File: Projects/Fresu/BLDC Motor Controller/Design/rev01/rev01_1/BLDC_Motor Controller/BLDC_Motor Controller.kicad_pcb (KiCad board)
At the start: 4 copper layers, 100 x 75 mm, 178 parts, among them CN1 XT60PW-M, J1 Conn_01x08, J2 Conn_01x06, J3 Conn_01x03, J4 7461084, J5 7461084, J6 7461084, J7 Conn_01x06, J8 XH-2PWBPZ, J9 TYPE-C-31-M-12, Q1 HSBA15810C, Q2 HSBA15810C, Q3 HSBA15810C, Q4 HSBA15810C, Q5 HSBA15810C, Q6 HSBA15810C, SW1 PTS526SK15SMTR2LFS, U1 STM32F405RGTx, U2 DRV8302_DCA_56, U3 S4B-XH-SM4-TB-(LF)(SN), U4 SN65HVD230, U5 AMS1117-3.3, U6 PUSB3AB6Z, Y1 8MHz

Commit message: Update 22
Continued DRC
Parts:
- C56: moved to B.Cu
- moved C56 0.78 mm to (238.6, 119.6)
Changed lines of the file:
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@@
     (pad "2" thru_hole circle locked (at 5.643701 0.113589 180) (size 2.2 2.2) (drill 1.2) (layers "*.Cu" "*.Mask")
       (net 2 "GND") (pinfunction "2") (pintype "passive"))
-    (model "C:/Users/Will/Downloads/Libraries (1)/Libraries/3D Models/CAP_LAT_SIDE.step"
+    (model "C:/Users/Will/Downloads/Libraries (1)/Libraries/3D Models/CAP_LAT_SIDE.step" hide
       (offset (xyz 1.9 -5.1 9.5))
       (scale (xyz 2.5 2.5 2.5))
@@
       (net 62 "H3_LOW") (pinfunction "2") (pintype "passive"))
   )
-  (footprint "DF_ESC_Footprint_Library:CAP-TH_BD18.0-P7.50-D1.2-SIDE" (layer "F.Cu")
-    (at 237.871 120.015 180)
-    (descr "CAP-TH_BD18.0-P7.50-D1.2-FD footprint")
-    (tags "CAP-TH_BD18.0-P7.50-D1.2-FD footprint")
-    (property "Capacitance" "820uF")
-    (property "LCSC" "C443097")
-    (property "Sheetfile" "INPUT PROTECTION.kicad_sch")
-    (property "Sheetname" "INPUT PROTECTION")
-    (property "ki_keywords" "C443097")
-    (attr through_hole)
-    (fp_text reference "C56" (at 2 -8.5) (layer "F.SilkS")
-        (effects (font (size 1 1) (thickness 0.15)))
-    )
-    (fp_text value "LKMI2501K821MF" (at 0 2.863602) (layer "F.Fab")
-        (effects (font (size 1 1) (thickness 0.15)))
-    )
-    (fp_text user "REF**" (at 0 4.863602) (layer "F.Fab")
-        (effects (font (size 1 1) (thickness 0.15)))
-    )
-    (fp_line (start -7.6 36) (end -7.6 4.5)
-      (stroke (width 0.12) (type solid)) (layer "F.SilkS"))
-    (fp_line (start -1.9 -2.536398) (end -1.9 -4.263602)
-      (stroke (width 0.254) (type solid)) (layer "F.SilkS"))
-    (fp_line (start -1.010998 -3.3746) (end -2.687402 -3.3746)
-      (stroke (width 0.254) (type solid)) (layer "F.SilkS"))
-    (fp_line (start 11.6 4.5) (end 11.604686 36)
-      (stroke (width 0.12) (type solid)) (layer "F.SilkS"))
-    (fp_line (start 11.6 36) (end -7.609372 36)
-      (stroke (width 0.12) (type solid)) (layer "F.SilkS"))
-    (fp_arc (start -7.6 4.5) (mid 2 -2.845853) (end 11.6 4.5)
-      (stroke (width 0.12) (type solid)) (layer "F.SilkS"))
-    (pad "1" thru_hole circle (at -1.856172 0.113589 180) (size 2.2 2.2) (drill 1.2) (layers "*.Cu" "*.Mask")
-      (net 18 "+VDC") (pinfunction "1") (pintype "passive"))
-    (pad "2" thru_hole circle (at 5.643701 0.113589 180) (size 2.2 2.2) (drill 1.2) (layers "*.Cu" "*.Mask")
-      (net 2 "GND") (pinfunction "2") (pintype "passive"))
-    (model "${DF_ESC_COURSE}/CAP_LAT_SIDE.step"
-      (offset (xyz 1.9 -5.1 9.5))
-      (scale (xyz 2.5 2.5 2.5))
-      (rotate (xyz -90 0 0))
-    )
-  )
   (footprint "DF_ESC_Footprint_Library:USB-C_SMD-TYPE-C-31-M-12" (layer "F.Cu")
     (at 216.748 103.08 180)
@@
     )
   )
+  (footprint "DF_ESC_Footprint_Library:CAP-TH_BD18.0-P7.50-D1.2-SIDE" (layer "B.Cu")
+    (at 238.561701 119.647411 180)
+    (descr "CAP-TH_BD18.0-P7.50-D1.2-FD footprint")
+    (tags "CAP-TH_BD18.0-P7.50-D1.2-FD footprint")
+    (property "Capacitance" "820uF")
+    (property "LCSC" "C443097")
+    (property "Sheetfile" "INPUT PROTECTION.kicad_sch")
+    (property "Sheetname" "INPUT PROTECTION")
+    (property "ki_keywords" "C443097")
+    (attr through_hole)
+    (fp_text reference "C56" (at 2 8.5) (layer "B.SilkS")
+        (effects (font (size 1 1) (thickness 0.15)) (justify mirror))
+    )
+    (fp_text value "LKMI2501K821MF" (at 0 -2.863602) (layer "B.Fab")
+        (effects (font (size 1 1) (thickness 0.15)) (justify mirror))
+    )
+    (fp_text user "REF**" (at 0 -4.863602) (layer "B.Fab")
+        (effects (font (size 1 1) (thickness 0.15)) (justify mirror))
+    )
+    (fp_line (start -7.6 -36) (end -7.6 -4.5)
+      (stroke (width 0.12) (type solid)) (layer "B.SilkS"))
+    (fp_line (start -1.9 2.536398) (end -1.9 4.263602)
+      (stroke (width 0.254) (type solid)) (layer "B.SilkS"))
+    (fp_line (start -1.010998 3.3746) (end -2.687402 3.3746)
+      (stroke (width 0.254) (type solid)) (layer "B.SilkS"))
+    (fp_line (start 11.6 -36) (end -7.609372 -36)
+      (stroke (width 0.12) (type solid)) (layer "B.SilkS"))
+    (fp_line (start 11.6 -4.5) (end 11.604686 -36)
+      (stroke (width 0.12) (type solid)) (layer "B.SilkS"))
+    (fp_arc (start 11.6 -4.5) (mid 2 2.845853) (end -7.6 -4.5)
+      (stroke (width 0.12) (type solid)) (layer "B.SilkS"))
+    (pad "1" thru_hole circle (at -1.856172 -0.113589 180) (size 2.2 2.2) (drill 1.2) (layers "*.Cu" "*.Mask")
+      (net 18 "+VDC") (pinfunction "1") (pintype "passive"))
+    (pad "2" thru_hole circle (at 5.643701 -0.113589 180) (size 2.2 2.2) (drill 1.2) (layers "*.Cu" "*.Mask")
+      (net 2 "GND") (pinfunction "2") (pintype "passive"))
+    (model "C:/Users/Will/Downloads/Libraries (1)/Libraries/3D Models/CAP_LAT_SIDE.step"
+      (offset (xyz 1.9 -5.1 9.5))
+      (scale (xyz 2.5 2.5 2.5))
+      (rotate (xyz -90 0 0))
+    )
+  )

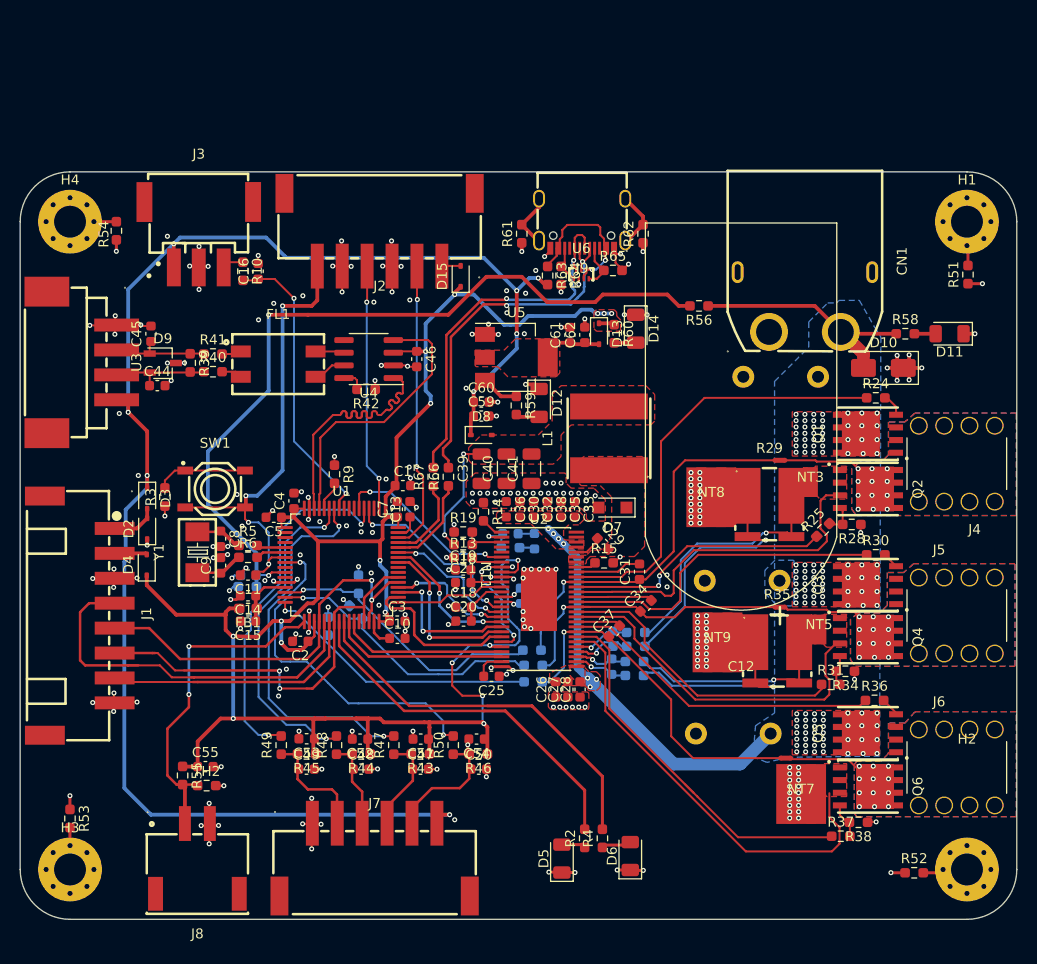
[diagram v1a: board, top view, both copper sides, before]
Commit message: Update 23
Converted to Kicad 8

Working on DRC
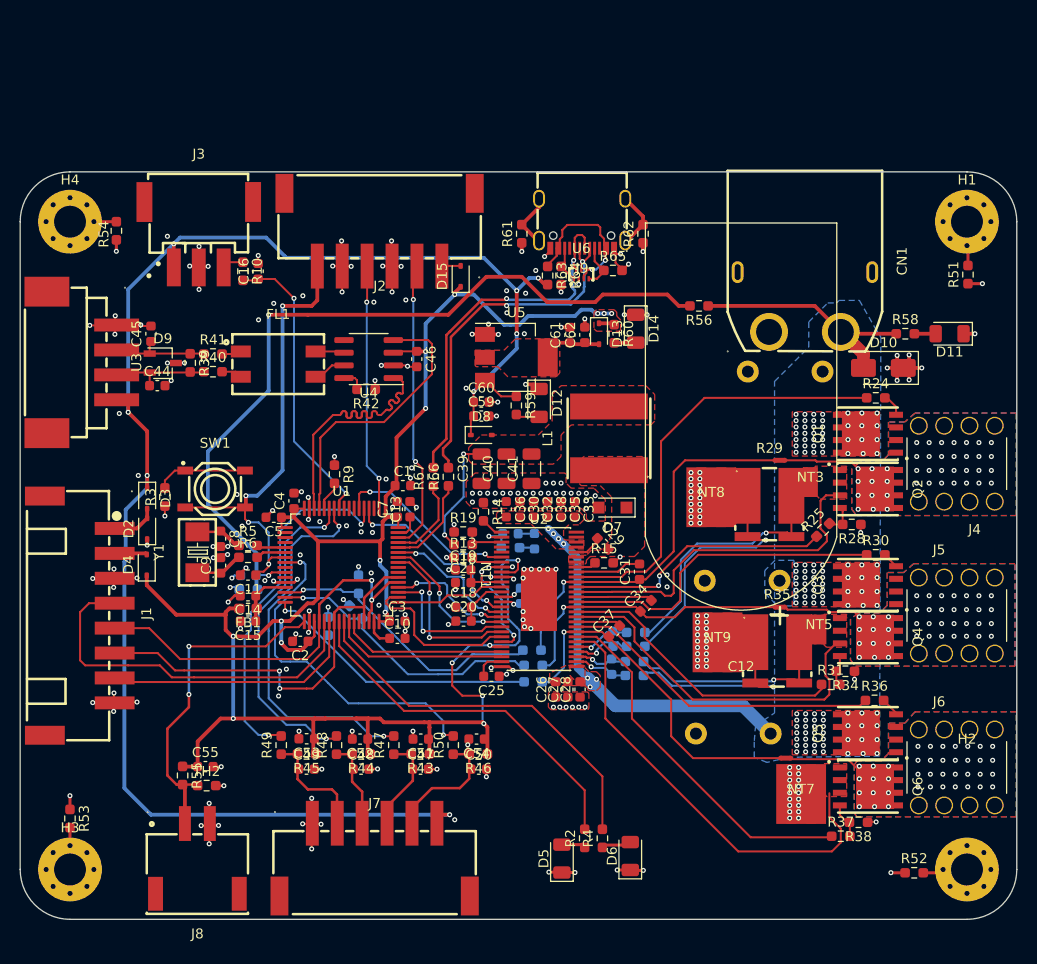
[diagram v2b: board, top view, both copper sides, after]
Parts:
- moved C56 0.69 mm to (239.0, 119.1)
- moved R57 0.30 mm to (183.3, 141.1)
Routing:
- net +VDC: track 64.5 -> 62.0 mm
- net M_L3: track 38.9 -> 36.9 mm
- net /MCU/SCK_ADC_EXT: track 39.3 -> 37.9 mm
- net H2_VS: track 30.7 -> 29.3 mm
- net H3_VS: track 36.8 -> 35.5 mm
- net SENS3: track 29.3 -> 28.5 mm
- net H3_LOW: track 44.4 -> 44.9 mm
- net /MCU/MISO_ADC_EXT2: track 26.8 -> 26.3 mm
- net M_L1: track 27.4 -> 26.8 mm
- net /MOSFETS/PHASE_3: vias 12 -> 40
- net /MOSFETS/PHASE_2: vias 12 -> 40
- net /MOSFETS/PHASE_1: vias 12 -> 40
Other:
- rule pad_to_mask_clearance: 0 -> 0.0762

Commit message: Update 24
DRC Complete
Generating MFR'ing files
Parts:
- moved R30 0.63 mm to (246.6, 137.2)
- moved R36 0.34 mm to (246.1, 151.9)
- moved D6 0.30 mm to (221.6, 168.1)
- moved C2 0.25 mm to (188.5, 146.6)
- moved R42 0.25 mm to (195.1, 121.3)
- moved C8 0.25 mm to (180.5, 135.8)
- moved R5 0.17 mm to (183.3, 136.5)
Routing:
- net AN_IN: track 80.6 -> 78.8 mm
- net H1_LOW: track 35.4 -> 33.7 mm
- net +3V3: track 204.8 -> 203.7 mm
- net GND: track 156.2 -> 155.1 mm, vias 252 -> 258
- net /FET Driver/+5V_DRV: track 12.1 -> 12.8 mm
- net /MOSFETS/SH1_N: track 25.6 -> 26.3 mm
- net M_H2: track 33.3 -> 33.9 mm
- net +5V: track 162.6 -> 163.0 mm, vias 8 -> 9
- net M_L1: track 26.8 -> 26.4 mm, vias 2 -> 0
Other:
- rule pad_to_mask_clearance: 0.0762 -> 0
- board text added: "02/25/2024"

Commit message: Update 25
Capturing all updates
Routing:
- net GND: vias 258 -> 526
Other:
- board text added: "0 mils"
- board text added: "0.3937007874 mils"
- board text added: "02/25/2024 1. FABRICATE PER IPC-6012A CLASS 2. 2. FOR BOARD THICKNESS AND IMPEDANCE DETAILS REFER STACKUP DOCUMENT. 3. PRINTED WIRING BOARD SHALL COMPLY WITH REQUIREMENTS OF ANSI/J-STD-003. 4. SURFACE FINISH: ENIG 5. SOLDERMASK ON BOTH SIDES OF THE BOARD SHALL BE LPI, COLOR GREEN. 6. SILK SCREEN LEGEND TO BE APPLIED PER LAYER STACKUP USING WHITE NON-CONDUCTIVE EPOXY INK. 7. THIS PRINTED WIRING BO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"
- board text added: "10 mils"
- board text added: "2.755905512 mils"
- board text added: "35 mils"
- board text added: "3937.01 mils x 2952.76 mils"
- board text added: "4"
- board text added: "66.81 mils"
- board text added: "8.00 mils"
- board text added: "8.00 mils / 8.00 mils"
- board text added: "Dielectric 1"
- board text added: "Dielectric 2"
- board text added: "Dielectric 3"
- board text added: "In1.Cu"
- board text added: "In2.Cu"
- board text added: "Thickness (mils)"
- board text added: "Yes"
- board text added: "prepreg"
- board text removed: "0 mm"
- board text removed: "0.01 mm"
- board text removed: "0.035 mm"
- board text removed: "0.2000 mm / 0.0000 mm"
- board text removed: "0.3000 mm"
- board text removed: "02/25/2024"
- board text removed: "1.51 mm"
- board text removed: "1.6000 mm"
- board text removed: "2"
- board text removed: "65.0000 mm x 56.0000 mm"
- board text removed: "Dielectric"
- board text removed: "Extend PCB edge 0.5mm if using SMT header"
- board text removed: "Thickness (mm)"

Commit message: Update 26
Matched DF's Designators to mine so I can use BOM as is

Updated MFR'ing files

Rev1 Ready for release
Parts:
- renumbered C56 to C1, C4 to C10, C5 to C11, C8 to C12, C9 to C13, C7 to C14, C10 to C16, C11 to C17, C13 to C18, C14 to C19, C58 to C2, C15 to C20, C16 to C21, C55 to C22, C19 to C23, C18 to C24, C22 to C25, C21 to C26, C20 to C27, C23 to C28, C24 to C29, C59 to C3, C25 to C30, C26 to C31, C27 to C32, C29 to C33, C28 to C34, C31 to C35, C30 to C36, C32 to C37, C33 to C38, C34 to C39, C60 to C4, C35 to C40, C36 to C41, C39 to C42, C37 to C43, C38 to C44, C42 to C45, C43 to C46, C44 to C47, C45 to C48, C46 to C49, C61 to C5, C47 to C50, C48 to C51, C49 to C52, C50 to C53, C51 to C54, C52 to C55, C53 to C56, C54 to C57, C57 to C58, C40 to C59, C62 to C6, C41 to C60, C1 to C7, C2 to C8, C3 to C9, C12 to C99, U6 to CR1, D10 to D1, D6 to D10, D15 to D11, D7 to D12, D8 to D13, D9 to D14, D12 to D15, D11 to D2, D13 to D3, D14 to D4, D2 to D5, D4 to D6, D3 to D8, D5 to D9, CN1 to J1, J9 to J10, J1 to J2, J2 to J3, J3 to J4, J4 to J5, J5 to J6, J6 to J7, U3 to J8, J7 to J9, R56 to R1, R55 to R11, R18 to R16, R19 to R17, R16 to R18, R17 to R19, R57 to R2, R25 to R24, R24 to R25, R58 to R3, R31 to R30, R30 to R31, R34 to R32, R37 to R33, R36 to R34, R32 to R35, R33 to R36, R38 to R37, R35 to R38, R60 to R4, R52 to R50, R53 to R52, R54 to R53, R62 to R54, R63 to R55, R64 to R56, R65 to R57, R61 to R60, R50 to R61, R59 to R62, R3 to R63, R2 to R7, R4 to R8, TH2 to TH1, U5 to U1, U1 to U2, U2 to U3, J8 to U5
